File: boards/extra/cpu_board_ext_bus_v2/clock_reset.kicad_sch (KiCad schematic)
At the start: 8 parts, among them J2 EXT_CLK, J3 CPU_CLK_SEL, J4 BUS_CLK_SEL, X1 INT_CLK

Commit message: Preparation for ordering with PCBWay.
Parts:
- C3: MPN (none) -> FG28X7R1H104KNT06; Manufacturer (none) -> TDK; Package (none) -> Plugin,P=5mm
- D1: MPN (none) -> 1N4148TA; Manufacturer (none) -> onsemi; Package (none) -> DO-35
- J2: MPN (none) -> PZ254R-11-02P; Manufacturer (none) -> XFCN; Package (none) -> Push-Pull,P=2.54mm
- J3, J4: MPN (none) -> PZ254R-11-03P; Manufacturer (none) -> XFCN; Package (none) -> Push-Pull,P=2.54mm
- R1, R2: MPN (none) -> MFR3WSFTE73-10K; Manufacturer (none) -> YAGEO; Package (none) -> Plugin
- X1: MPN (none) -> 1-2199298-2; Manufacturer (none) -> TE Connectivity; Package (none) -> DIP-8
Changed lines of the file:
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@@
+      (effects (font (size 1.27 1.27)) hide)
+    )
+    (property "Description" "Phosphor bronze 7.62mm DIP-8 IC / Transistor Socket ROHS " (at 141.605 98.425 0)
+      (effects (font (size 1.27 1.27)) hide)
+    )
+    (property "MPN" "1-2199298-2" (at 141.605 98.425 0)
+      (effects (font (size 1.27 1.27)) hide)
+    )
+    (property "Manufacturer" "TE Connectivity " (at 141.605 98.425 0)
+      (effects (font (size 1.27 1.27)) hide)
+    )
+    (property "Package" "DIP-8" (at 141.605 98.425 0)
       (effects (font (size 1.27 1.27)) hide)
     )
@@
       (effects (font (size 1.27 1.27)) hide)
     )
+    (property "Description" "Metal Film Resistors 10kΩ 3W ±50ppm/℃ ±1% Plugin Through Hole Resistors ROHS " (at 176.53 43.815 0)
+      (effects (font (size 1.27 1.27)) hide)
+    )
+    (property "MPN" "MFR3WSFTE73-10K" (at 176.53 43.815 0)
+      (effects (font (size 1.27 1.27)) hide)
+    )
+    (property "Manufacturer" "YAGEO" (at 176.53 43.815 0)
+      (effects (font (size 1.27 1.27)) hide)
+    )
+    (property "Package" "Plugin" (at 176.53 43.815 0)
+      (effects (font (size 1.27 1.27)) hide)
+    )
     (pin "1")
     (pin "2")
@@
     )
     (property "Datasheet" "~" (at 184.15 53.975 0)
+      (effects (font (size 1.27 1.27)) hide)
+    )
+    (property "Description" " 	±10% 50V 100nF X7R Plugin,P=5mm Multilayer Ceramic Capacitors MLCC - Leaded ROHS " (at 184.15 53.975 0)
+      (effects (font (size 1.27 1.27)) hide)
+    )
+    (property "MPN" "FG28X7R1H104KNT06" (at 184.15 53.975 0)
+      (effects (font (size 1.27 1.27)) hide)
+    )
+    (property "Manufacturer" "TDK" (at 184.15 53.975 0)
+      (effects (font (size 1.27 1.27)) hide)
+    )
+    (property "Package" " Plugin,P=5mm" (at 184.15 53.975 0)
       (effects (font (size 1.27 1.27)) hide)
     )
@@
       (effects (font (size 1.27 1.27)) hide)
     )
+    (property "Description" "Right-Angle Square Pins 2.5mm 3P 6mm -40℃~+105℃ 2.54mm Plugin Black Brass 1x3P Push-Pull,P=2.54mm Pin Headers ROHS " (at 31.115 57.15 0)
+      (effects (font (size 1.27 1.27)) hide)
+    )
+    (property "MPN" "PZ254R-11-03P " (at 31.115 57.15 0)
+      (effects (font (size 1.27 1.27)) hide)
+    )
+    (property "Manufacturer" "XFCN" (at 31.115 57.15 0)
+      (effects (font (size 1.27 1.27)) hide)
+    )
+    (property "Package" "Push-Pull,P=2.54mm" (at 31.115 57.15 0)
+      (effects (font (size 1.27 1.27)) hide)
+    )
     (pin "1")
     (pin "2")
@@
       (effects (font (size 1.27 1.27)) hide)
     )
+    (property "Description" "100V 1V@10mA 4ns 200mA DO-35 Switching Diode ROHS " (at 176.53 33.655 0)
+      (effects (font (size 1.27 1.27)) hide)
+    )
+    (property "MPN" "1N4148TA" (at 176.53 33.655 0)
+      (effects (font (size 1.27 1.27)) hide)
+    )
+    (property "Manufacturer" "onsemi " (at 176.53 33.655 0)
+      (effects (font (size 1.27 1.27)) hide)
+    )
+    (property "Package" "DO-35" (at 176.53 33.655 0)
+      (effects (font (size 1.27 1.27)) hide)
+    )
     (pin "1")
     (pin "2")
@@
     )
     (property "Datasheet" "~" (at 154.94 33.655 0)
+      (effects (font (size 1.27 1.27)) hide)
+    )
+    (property "Description" "Metal Film Resistors 10kΩ 3W ±50ppm/℃ ±1% Plugin Through Hole Resistors ROHS " (at 154.94 33.655 0)
+      (effects (font (size 1.27 1.27)) hide)
+    )
+    (property "MPN" "MFR3WSFTE73-10K" (at 154.94 33.655 0)
+      (effects (font (size 1.27 1.27)) hide)
+    )
+    (property "Manufacturer" "YAGEO" (at 154.94 33.655 0)
+      (effects (font (size 1.27 1.27)) hide)
+    )
+    (property "Package" "Plugin" (at 154.94 33.655 0)
       (effects (font (size 1.27 1.27)) hide)
     )
@@
       (effects (font (size 1.27 1.27)) hide)
     )
+    (property "Description" "Right-Angle Square Pins 2.5mm 3P 6mm -40℃~+105℃ 2.54mm Plugin Black Brass 1x3P Push-Pull,P=2.54mm Pin Headers ROHS " (at 31.115 67.945 0)
+      (effects (font (size 1.27 1.27)) hide)
+    )
+    (property "MPN" "PZ254R-11-03P" (at 31.115 67.945 0)
+      (effects (font (size 1.27 1.27)) hide)
+    )
+    (property "Manufacturer" "XFCN" (at 31.115 67.945 0)
+      (effects (font (size 1.27 1.27)) hide)
+    )
+    (property "Package" "Push-Pull,P=2.54mm" (at 31.115 67.945 0)
+      (effects (font (size 1.27 1.27)) hide)
+    )
     (pin "1")
     (pin "2")
@@
       (effects (font (size 1.27 1.27)) hide)
     )
+    (property "Description" "Right-Angle Square Pins 2.5mm 2P 6mm -40℃~+105℃ 2.54mm Plugin Black Brass 1x2P Push-Pull,P=2.54mm Pin Headers ROHS " (at 31.115 40.005 0)
+      (effects (font (size 1.27 1.27)) hide)
+    )
+    (property "MPN" "PZ254R-11-02P" (at 31.115 40.005 0)
+      (effects (font (size 1.27 1.27)) hide)
+    )
+    (property "Manufacturer" "XFCN" (at 31.115 40.005 0)
+      (effects (font (size 1.27 1.27)) hide)
+    )
+    (property "Package" "Push-Pull,P=2.54mm" (at 31.115 40.005 0)
+      (effects (font (size 1.27 1.27)) hide)
+    )

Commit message: Changed footprint of D2 to DO-35.
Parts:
- D1: footprint Diode_THT:D_A-405_P7.62mm_Horizontal -> Diode_THT:D_DO-35_SOD27_P7.62mm_Horizontal
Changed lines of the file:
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@@
       (effects (font (size 1.27 1.27)))
     )
-    (property "Footprint" "Diode_THT:D_A-405_P7.62mm_Horizontal" (at 176.53 33.655 0)
+    (property "Footprint" "Diode_THT:D_DO-35_SOD27_P7.62mm_Horizontal" (at 176.53 33.655 0)
       (effects (font (size 1.27 1.27)) hide)
     )

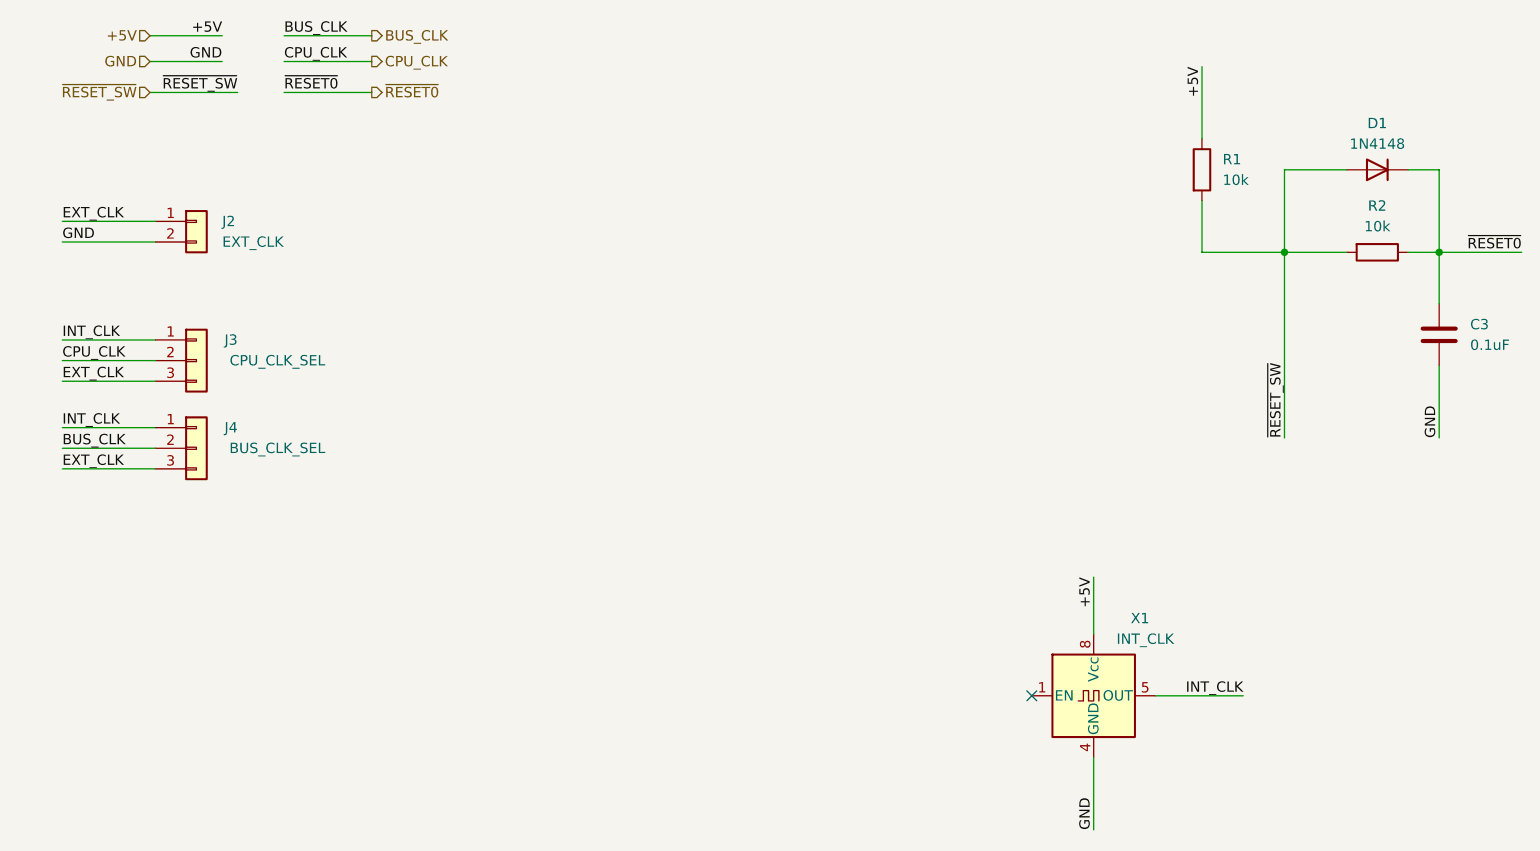
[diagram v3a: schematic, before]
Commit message: Upgraded board to KiCad 8 and imported design rules from the PCBWay website.
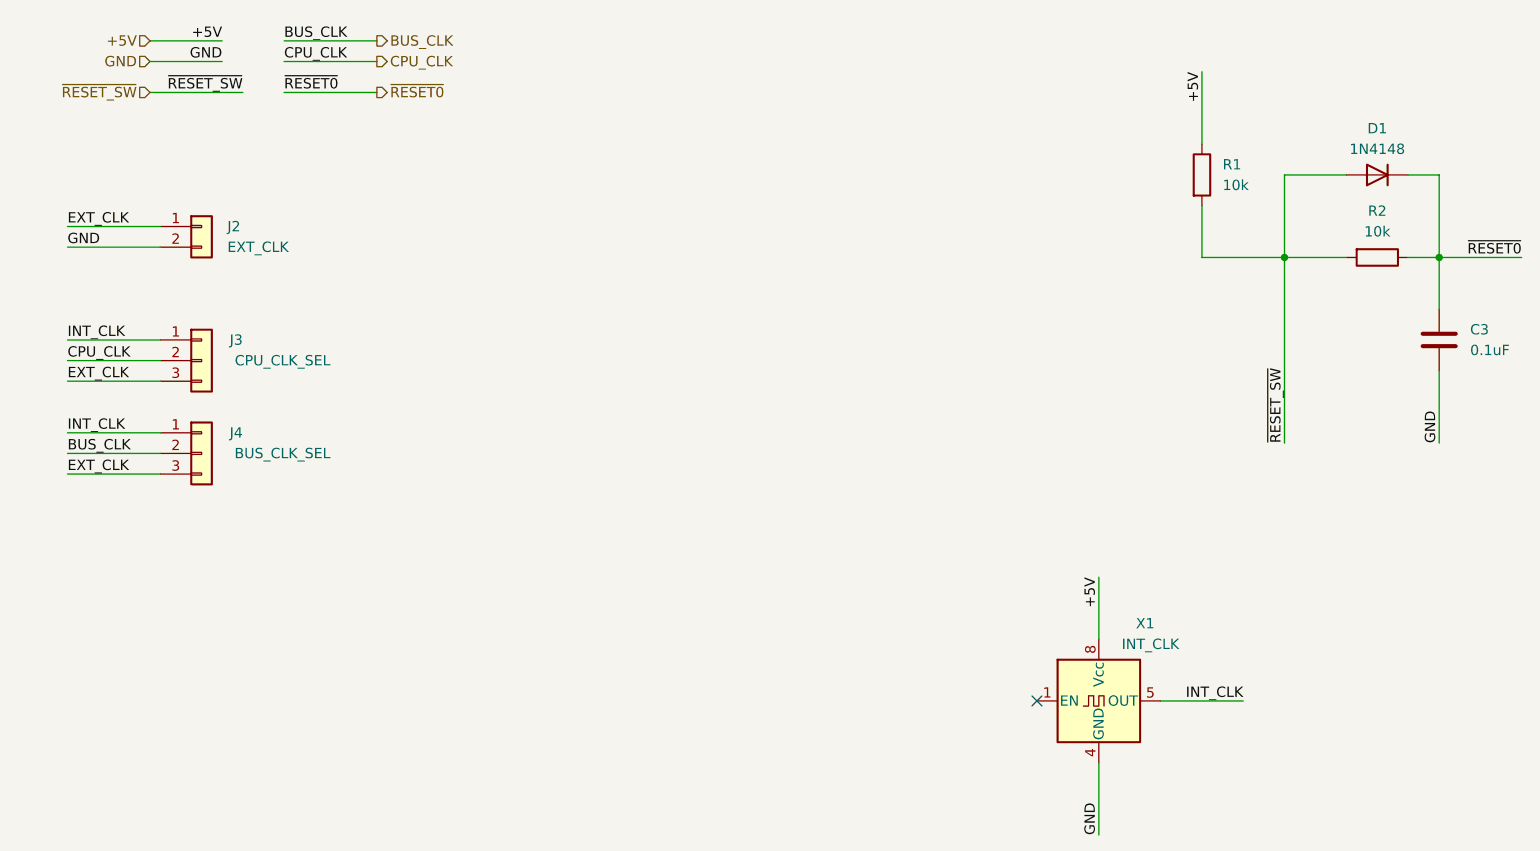
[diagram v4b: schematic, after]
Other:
- moved on the sheet: C3, D1, J2, J3, J4, R1, R2, X1
